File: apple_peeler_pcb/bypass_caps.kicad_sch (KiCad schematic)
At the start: 12 parts

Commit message: some progress
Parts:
- removed C20: 100nF, Capacitor_SMD:C_0805_2012Metric, symbol Device:C_Small
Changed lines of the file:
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@@
-	)
-	(junction
-		(at 168.91 59.69)
-		(diameter 0)
-		(color 0 0 0 0)
 	)
 	(junction
@@
 	(wire
 		(pts
-			(xy 157.48 59.69) (xy 168.91 59.69)
+			(xy 157.48 59.69) (xy 180.34 59.69)
 		)
 		(stroke
@@
 	(wire
 		(pts
-			(xy 168.91 60.96) (xy 168.91 59.69)
-		)
-		(stroke
-			(width 0)
-			(type default)
-		)
-	)
-	(wire
-		(pts
 			(xy 83.82 60.96) (xy 83.82 59.69)
 		)
@@
 	(wire
 		(pts
-			(xy 168.91 66.04) (xy 168.91 67.31)
-		)
-		(stroke
-			(width 0)
-			(type default)
-		)
-	)
-	(wire
-		(pts
 			(xy 93.98 66.04) (xy 93.98 67.31)
 		)
@@
 		(pts
 			(xy 76.2 59.69) (xy 83.82 59.69)
-		)
-		(stroke
-			(width 0)
-			(type default)
-		)
-	)
-	(wire
-		(pts
-			(xy 168.91 59.69) (xy 180.34 59.69)
 		)
 		(stroke
@@
 	)
 	(symbol
-		(lib_id "Device:C_Small")
-		(at 168.91 63.5 0)
-		(mirror y)
-		(unit 1)
-		(exclude_from_sim no)
-		(in_bom yes)
-		(on_board yes)
-		(dnp no)
-		(property "Reference" "C20"
-			(at 166.37 62.2362 0)
-			(effects
-				(font
-					(size 1.27 1.27)
-				)
-				(justify left)
-			)
-		)
-		(property "Value" "100nF"
-			(at 166.37 64.7762 0)
-			(effects
-				(font
-					(size 1.27 1.27)
-				)
-				(justify left)
-			)
-		)
-		(property "Footprint" "Capacitor_SMD:C_0805_2012Metric"
-			(at 168.91 63.5 0)
-			(effects
-				(font
-					(size 1.27 1.27)
-				)
-				(hide yes)
-			)
-		)
-		(property "Datasheet" "~"
-			(at 168.91 63.5 0)
-			(effects
-				(font
-					(size 1.27 1.27)
-				)
-				(hide yes)
-			)
-		)
-		(property "Description" "Unpolarized capacitor, small symbol"
-			(at 168.91 63.5 0)
-			(effects
-				(font
-					(size 1.27 1.27)
-				)
-				(hide yes)
-			)
-		)
-		(property "LCSC" "C49678"
-			(at 168.91 63.5 0)
-			(effects
-				(font
-					(size 1.27 1.27)
-				)
-				(hide yes)
-			)
-		)
-		(property "MPN" "C 100nF 50V 0805"
-			(at 168.91 63.5 0)
-			(effects
-				(font
-					(size 1.27 1.27)
-				)
-				(hide yes)
-			)
-		)
-		(property "Pin" "43"
-			(at 168.91 57.912 0)
-			(show_name yes)
-			(effects
-				(font
-					(size 1.27 1.27)
-				)
-			)
-		)
-		(pin "2"
-		)
-		(pin "1"
-		)
-		(instances
-			(project ""
-				(path "/d5946b96-44a8-4a28-8641-19803e1510af/36c29319-2fb9-4e97-8e03-94576ed291d6"
-					(reference "C20")
-					(unit 1)
-				)
-			)
-		)
-	)
-	(symbol
 		(lib_id "power:+3.3V")
 		(at 105.41 97.79 0)
@@
 					(unit 1)
 				)
-			)
-		)
-	)
-	(symbol
-		(lib_id "power:GND")
-		(at 168.91 67.31 0)
-		(unit 1)
-		(exclude_from_sim no)
-		(in_bom yes)
-		(on_board yes)
-		(dnp no)
-		(fields_autoplaced yes)
-		(property "Reference" "#PWR079"
-			(at 168.91 73.66 0)
-			(effects
-				(font
-					(size 1.27 1.27)
-				)
-				(hide yes)
-			)
-		)
-		(property "Value" "GND"
-			(at 168.91 72.39 0)
-			(effects
-				(font
-					(size 1.27 1.27)
-				)
-				(hide yes)
-			)
-		)
-		(property "Footprint" ""
-			(at 168.91 67.31 0)
-			(effects
-				(font
-					(size 1.27 1.27)
-				)
-				(hide yes)
-			)
-		)
-		(property "Datasheet" ""
-			(at 168.91 67.31 0)
-			(effects
-				(font
-					(size 1.27 1.27)
-				)
-				(hide yes)
-			)
-		)
-		(property "Description" "Power symbol creates a global label with name \"GND\" , ground"
-			(at 168.91 67.31 0)
-			(effects
-				(font
-					(size 1.27 1.27)
-				)
-				(hide yes)
-			)
-		)
-		(pin "1"
-		)
-		(instances
-			(project ""
-				(path "/d5946b96-44a8-4a28-8641-19803e1510af/36c29319-2fb9-4e97-8e03-94576ed291d6"
-					(reference "#PWR079")
-					(unit 1)
-				)

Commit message: make space for bypass cap near switch chip
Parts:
- added C?: 2.2μF, Capacitor_SMD:C_0805_2012Metric, symbol Device:C_Small
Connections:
- net +3.3V: now also C?.1
- net GND: now also C?.2

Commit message: reannotate schematic
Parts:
- gave numbers to parts that had none: 1
- renumbered C17 to C18, C18 to C19, C19 to C20
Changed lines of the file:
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@@
+		(dnp no)
+		(fields_autoplaced yes)
+		(property "Reference" "#PWR079"
+			(at 146.05 73.66 0)
+			(effects
+				(font
+					(size 1.27 1.27)
+				)
+				(hide yes)
+			)
+		)
+		(property "Value" "GND"
+			(at 146.05 72.39 0)
+			(effects
+				(font
+					(size 1.27 1.27)
+				)
+				(hide yes)
+			)
+		)
+		(property "Footprint" ""
+			(at 146.05 67.31 0)
+			(effects
+				(font
+					(size 1.27 1.27)
+				)
+				(hide yes)
+			)
+		)
+		(property "Datasheet" ""
+			(at 146.05 67.31 0)
+			(effects
+				(font
+					(size 1.27 1.27)
+				)
+				(hide yes)
+			)
+		)
+		(property "Description" "Power symbol creates a global label with name \"GND\" , ground"
+			(at 146.05 67.31 0)
+			(effects
+				(font
+					(size 1.27 1.27)
+				)
+				(hide yes)
+			)
+		)
+		(pin "1"
+		)
+		(instances
+			(project ""
+				(path "/d5946b96-44a8-4a28-8641-19803e1510af/36c29319-2fb9-4e97-8e03-94576ed291d6"
+					(reference "#PWR079")
+					(unit 1)
+				)
+			)
+		)
+	)
+	(symbol
+		(lib_id "power:GND")
+		(at 127 105.41 0)
+		(unit 1)
+		(exclude_from_sim no)
+		(in_bom yes)
+		(on_board yes)
 		(dnp no)
 		(fields_autoplaced yes)
 		(property "Reference" "#PWR077"
-			(at 146.05 73.66 0)
-			(effects
-				(font
-					(size 1.27 1.27)
-				)
-				(hide yes)
-			)
-		)
-		(property "Value" "GND"
-			(at 146.05 72.39 0)
-			(effects
-				(font
-					(size 1.27 1.27)
-				)
-				(hide yes)
-			)
-		)
-		(property "Footprint" ""
-			(at 146.05 67.31 0)
-			(effects
-				(font
-					(size 1.27 1.27)
-				)
-				(hide yes)
-			)
-		)
-		(property "Datasheet" ""
-			(at 146.05 67.31 0)
-			(effects
-				(font
-					(size 1.27 1.27)
-				)
-				(hide yes)
-			)
-		)
-		(property "Description" "Power symbol creates a global label with name \"GND\" , ground"
-			(at 146.05 67.31 0)
-			(effects
-				(font
-					(size 1.27 1.27)
-				)
-				(hide yes)
-			)
-		)
-		(pin "1"
-		)
-		(instances
-			(project ""
-				(path "/d5946b96-44a8-4a28-8641-19803e1510af/36c29319-2fb9-4e97-8e03-94576ed291d6"
-					(reference "#PWR077")
-					(unit 1)
-				)
-			)
-		)
-	)
-	(symbol
-		(lib_id "power:GND")
-		(at 127 105.41 0)
-		(unit 1)
-		(exclude_from_sim no)
-		(in_bom yes)
-		(on_board yes)
-		(dnp no)
-		(fields_autoplaced yes)
-		(property "Reference" "#PWR0115"
 			(at 127 111.76 0)
 			(effects
@@
 			(project "apple_peeler_pcb"
 				(path "/d5946b96-44a8-4a28-8641-19803e1510af/36c29319-2fb9-4e97-8e03-94576ed291d6"
-					(reference "#PWR0115")
+					(reference "#PWR077")
 					(unit 1)
 				)
@@
 		(dnp no)
 		(fields_autoplaced yes)
-		(property "Reference" "#PWR076"
+		(property "Reference" "#PWR078"
 			(at 134.62 73.66 0)
 			(effects
@@
 			(project ""
 				(path "/d5946b96-44a8-4a28-8641-19803e1510af/36c29319-2fb9-4e97-8e03-94576ed291d6"
-					(reference "#PWR076")
+					(reference "#PWR078")
 					(unit 1)
 				)
@@
 		(on_board yes)
 		(dnp no)
-		(property "Reference" "C19"
+		(property "Reference" "C20"
 			(at 154.94 62.2362 0)
 			(effects
@@
 			(project ""
 				(path "/d5946b96-44a8-4a28-8641-19803e1510af/36c29319-2fb9-4e97-8e03-94576ed291d6"
-					(reference "C19")
+					(reference "C20")
 					(unit 1)
 				)
@@
 		(dnp no)
 		(fields_autoplaced yes)
-		(property "Reference" "#PWR082"
+		(property "Reference" "#PWR083"
 			(at 203.2 73.66 0)
 			(effects
@@
 			(project ""
 				(path "/d5946b96-44a8-4a28-8641-19803e1510af/36c29319-2fb9-4e97-8e03-94576ed291d6"
-					(reference "#PWR082")
+					(reference "#PWR083")
 					(unit 1)
 				)
@@
 		(on_board yes)
 		(dnp no)
-		(property "Reference" "C17"
+		(property "Reference" "C18"
 			(at 132.08 62.2362 0)
 			(effects
@@
 			(project ""
 				(path "/d5946b96-44a8-4a28-8641-19803e1510af/36c29319-2fb9-4e97-8e03-94576ed291d6"
-					(reference "C17")
+					(reference "C18")
 					(unit 1)
 				)
@@
 		(dnp no)
 		(fields_autoplaced yes)
-		(property "Reference" "#PWR078"
+		(property "Reference" "#PWR080"
 			(at 157.48 73.66 0)
 			(effects
@@
 			(project ""
 				(path "/d5946b96-44a8-4a28-8641-19803e1510af/36c29319-2fb9-4e97-8e03-94576ed291d6"
-					(reference "#PWR078")
+					(reference "#PWR080")
 					(unit 1)
 				)
@@
 		(dnp no)
 		(fields_autoplaced yes)
-		(property "Reference" "#PWR080"
+		(property "Reference" "#PWR081"
 			(at 180.34 73.66 0)
 			(effects
@@
 			(project ""
 				(path "/d5946b96-44a8-4a28-8641-19803e1510af/36c29319-2fb9-4e97-8e03-94576ed291d6"
-					(reference "#PWR080")
+					(reference "#PWR081")
 					(unit 1)
 				)
@@
 		(on_board yes)
 		(dnp no)
-		(property "Reference" "C18"
+		(property "Reference" "C19"
 			(at 143.51 62.2362 0)
 			(effects
@@
 			(project ""
 				(path "/d5946b96-44a8-4a28-8641-19803e1510af/36c29319-2fb9-4e97-8e03-94576ed291d6"
-					(reference "C18")
+					(reference "C19")
 					(unit 1)
 				)
@@
 		(dnp no)
 		(fields_autoplaced yes)
-		(property "Reference" "#PWR079"
+		(property "Reference" "#PWR076"
 			(at 127 101.6 0)
 			(effects
@@
 			(project "apple_peeler_pcb"
 				(path "/d5946b96-44a8-4a28-8641-19803e1510af/36c29319-2fb9-4e97-8e03-94576ed291d6"
-					(reference "#PWR079")
+					(reference "#PWR076")
 					(unit 1)
 				)
@@
 		(dnp no)
 		(fields_autoplaced yes)
-		(property "Reference" "#PWR081"
+		(property "Reference" "#PWR082"
 			(at 191.77 73.66 0)
 			(effects
@@
 			(project ""
 				(path "/d5946b96-44a8-4a28-8641-19803e1510af/36c29319-2fb9-4e97-8e03-94576ed291d6"
-					(reference "#PWR081")
+					(reference "#PWR082")
 					(unit 1)
 				)
@@
 		(on_board yes)
 		(dnp no)
-		(property "Reference" "C?"
+		(property "Reference" "C17"
 			(at 124.46 100.3362 0)
 			(effects
@@
 			(project "apple_peeler_pcb"
 				(path "/d5946b96-44a8-4a28-8641-19803e1510af/36c29319-2fb9-4e97-8e03-94576ed291d6"
-					(reference "C?")
-					(unit 1)
-				)
+					(reference "C17")
+					(unit 1)
+				)

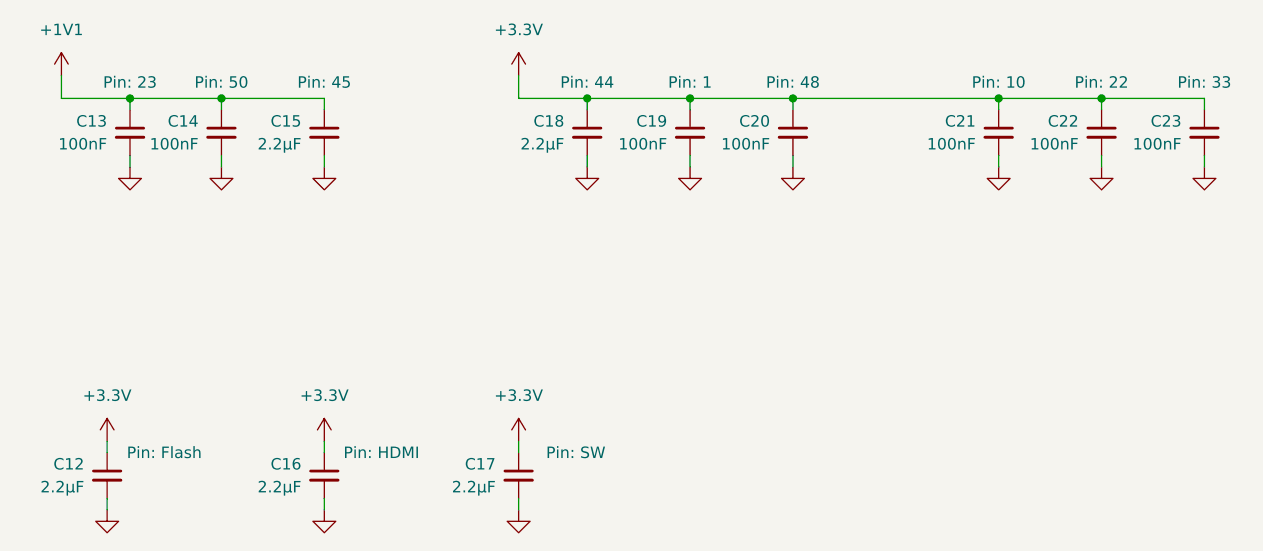
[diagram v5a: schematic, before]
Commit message: route all power traces
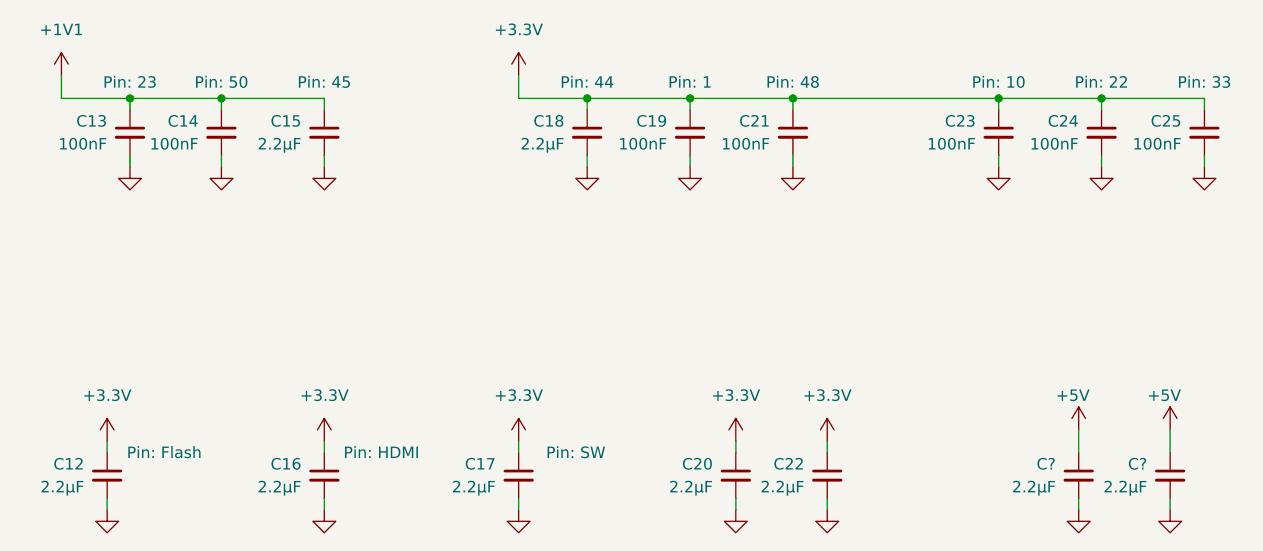
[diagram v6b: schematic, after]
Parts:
- added C20, C22, C? (x2): 2.2μF, Capacitor_SMD:C_0805_2012Metric, symbol Device:C_Small
- renumbered C20 to C21, C21 to C23, C22 to C24, C23 to C25
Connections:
- net +3.3V: now also C20.1, C22.1
- net GND: now also C20.2, C22.2, C?.2, C?.2
- new net +5V: C?.1, C?.1
